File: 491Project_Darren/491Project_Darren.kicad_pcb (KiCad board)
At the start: 4 copper layers, 77 x 77 mm, 51 parts, among them J1 RJ45, J2 RJ45

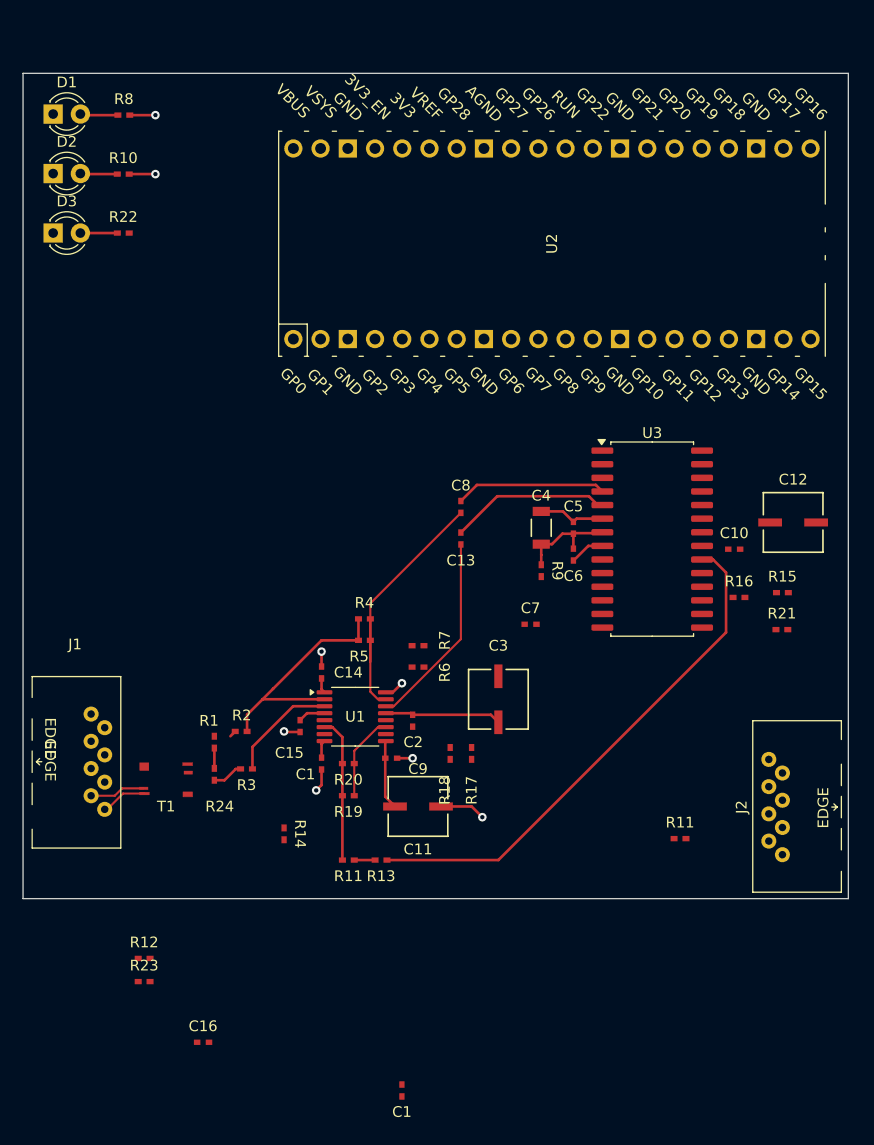
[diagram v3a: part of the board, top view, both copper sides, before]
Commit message: Added Power planes, Removed dead copper?
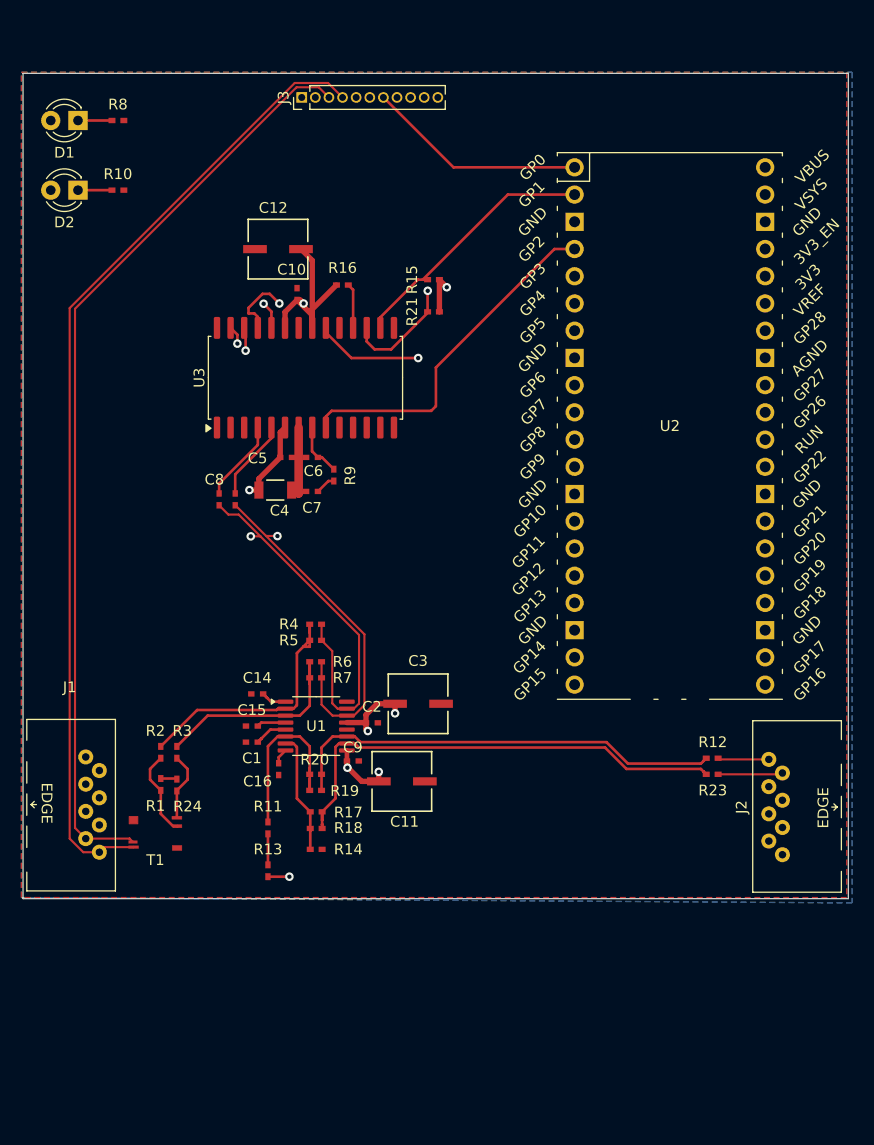
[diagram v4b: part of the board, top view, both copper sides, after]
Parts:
- removed the C1 at (142.5, 158.0)
- removed the C1 at (135.0, 127.5)
- removed D3: RED, LED_THT:LED_D3.0mm
- removed the R11 at (137.5, 136.5)
- removed R22: 1k, 491_Footprints:R_805
- added C1: 100nF, 491_Footprints:CAP_805_CER, F.Cu at (128.5, 125.5)
- added J3: Conn_01x10_MountingPin, Connector_PinHeader_1.27mm:PinHeader_1x11_P1.27mm_Vertical, F.Cu at (133.2, 65.3)
- R11: value 1k -> 100
- moved R23 56.4 mm to (171.4, 128.5)
- moved R12 56.2 mm to (171.4, 127.0)
- moved C12 54.4 mm to (130.9, 79.5), turned to 180 degrees
- moved C10 47.2 mm to (132.7, 83.7), turned to 90 degrees
- moved R16 47.1 mm to (136.9, 82.8), turned to 180 degrees
- moved R21 44.0 mm to (145.4, 85.3)
- moved R15 43.7 mm to (145.4, 82.3)
- moved R11 38.5 mm to (130.0, 133.5), turned to 90 degrees
- moved U3 35.7 mm to (133.5, 91.5), turned to 90 degrees
- moved C5 27.6 mm to (131.7, 98.9), turned to 0 degrees
- moved C16 26.4 mm to (131.0, 128.0), turned to -90 degrees
- moved C6 26.0 mm to (134.1, 98.9), turned to 180 degrees
- moved C4 25.1 mm to (130.7, 102.0), turned to 0 degrees
- moved C7 23.9 mm to (134.1, 102.1), turned to 180 degrees
- moved C8 22.6 mm to (125.4, 102.8)
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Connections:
- C7 pad 1: FILT -> Net-(C7-Pad1)
- C7 pad 2: Net-(C7-Pad2) -> GNDA
- D1 pad 1: GND -> Net-(D1-K)
- D1 pad 2: Net-(D1-A) -> +5V
- D2 pad 1: GND -> Net-(D2-K)
- D2 pad 2: Net-(D2-A) -> LED
- R10 pad 1: +5V -> Net-(D2-K)
- R10 pad 2: Net-(D2-A) -> GND
- R11 pad 1: +3V3 -> Net-(R11-Pad1)
- R11 pad 2: VCOM -> Net-(U1B-IN+)
- R8 pad 1: +5V -> Net-(D1-K)
- R8 pad 2: Net-(D1-A) -> GND
- R9 pad 1: GNDA -> Net-(C7-Pad1)
- R9 pad 2: Net-(C7-Pad2) -> FILT
- U1 pad 5: unconnected-(U1B-~{PD}-Pad5) -> Net-(U1B-~{PD})
- U2 pad 21: OLRCLK -> OSCLK
- U2 pad 22: OSCLK -> OLRCLK
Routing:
- net SIG_OUT+: track 0.00 -> 145.9 mm
- net SIG_OUT-: track 0.00 -> 142.2 mm
- net VA: track 6.26 -> 101.3 mm, vias 0 -> 1
- net SIG_IN-: track 4.31 -> 90.9 mm
- net SIG_IN+: track 5.19 -> 87.3 mm
- net LED: track 0.00 -> 77.3 mm
- net OSCLK: track 0.00 -> 76.5 mm, vias 0 -> 1
- net SDOUT: track 0.00 -> 72.7 mm, vias 0 -> 1
- net SDA: track 0.00 -> 51.1 mm, vias 0 -> 1
- net AES3-: track 18.4 -> 66.0 mm, vias 0 -> 1
- net AES3+: track 25.9 -> 72.6 mm, vias 0 -> 1
- net Net-(U1B-OUT+): track 0.00 -> 45.6 mm
- net PASS+: track 48.8 -> 93.5 mm, vias 0 -> 2
- net SCL: track 0.00 -> 44.6 mm
- net OMCLK: track 0.00 -> 34.9 mm, vias 0 -> 1
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- added copper zone on B.Cu, net +5V
- added copper zone on F.Cu, net GND
- removed copper zone on In2.Cu, net +5V
- removed copper zone on In1.Cu, net GND
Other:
- board text removed: "EDGE"

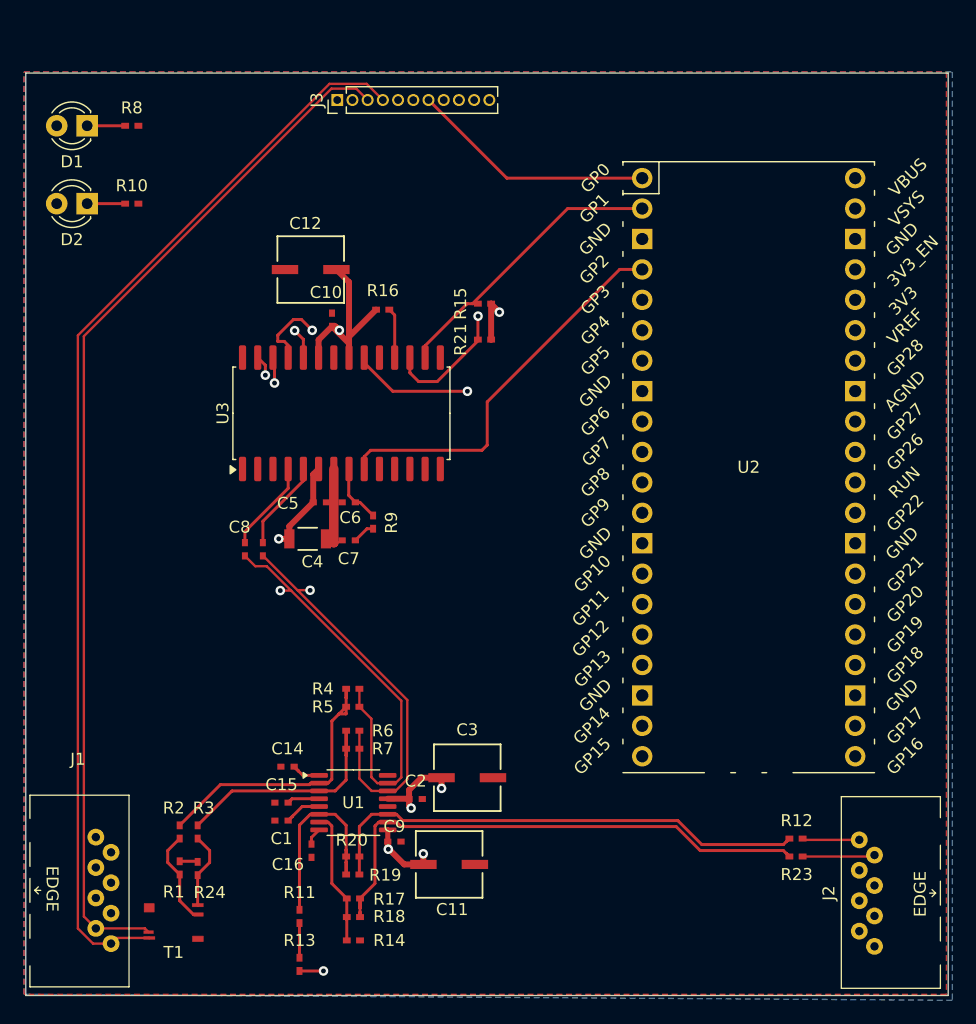
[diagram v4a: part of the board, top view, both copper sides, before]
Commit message: fix cutouts
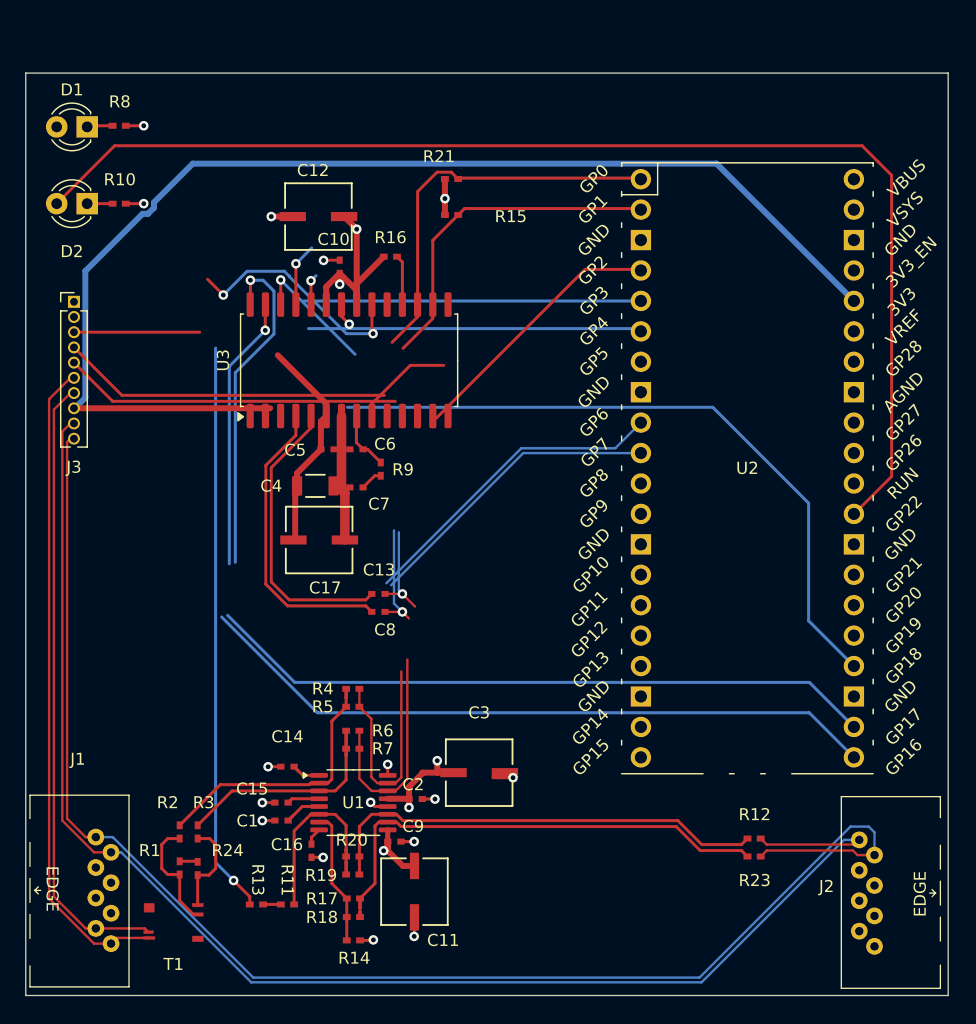
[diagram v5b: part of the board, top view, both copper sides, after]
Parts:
- added C17: 10uF, 491_Footprints:CAP_ALUM, F.Cu at (131.6, 102.1)
- J3: footprint Connector_PinHeader_1.27mm:PinHeader_1x11_P1.27mm_Vertical -> Connector_PinHeader_1.27mm:PinHeader_1x10_P1.27mm_Vertical
- moved J3 27.7 mm to (111.2, 82.2), turned to 0 degrees
- moved R21 13.7 mm to (142.7, 71.9), turned to 180 degrees
- moved C8 12.3 mm to (136.6, 108.1), turned to 180 degrees
- moved C13 10.3 mm to (136.6, 106.6), turned to 180 degrees
- moved R15 7.90 mm to (142.7, 74.9), turned to 180 degrees
- moved R13 6.16 mm to (126.4, 132.5), turned to 0 degrees
- moved C6 4.47 mm to (134.8, 94.5)
- moved C7 4.47 mm to (134.8, 97.7)
- moved C10 4.47 mm to (133.4, 79.3)
- moved C5 4.47 mm to (132.3, 94.5)
- moved R9 4.47 mm to (136.8, 96.2)
- moved U3 4.47 mm to (134.1, 87.1)
- moved C4 4.47 mm to (131.3, 97.6)
- moved R16 4.47 mm to (137.6, 78.4)
- moved C12 4.47 mm to (131.6, 75.1)
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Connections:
- J3 pad 1: VA -> unconnected-(J3-Pin_1-Pad1)
- J3 pad 10: unconnected-(J3-Pin_10-Pad10) -> SIG_OUT+
- J3 pad 3: SIG_IN+ -> PASS+
- J3 pad 4: SIG_IN- -> SDA
- J3 pad 5: SIG_OUT+ -> SCL
- J3 pad 6: SIG_OUT- -> SIG_IN-
- J3 pad 7: SDA -> SIG_IN+
- J3 pad 8: SCL -> VA
- J3 pad 9: PASS+ -> SIG_OUT-
- U2 pad 22: OLRCLK -> OLRCK
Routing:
- net OLRCK: track 0.00 -> 84.5 mm, vias 0 -> 1
- net SIG_IN-: track 90.9 -> 54.5 mm
- net SIG_IN+: track 87.3 -> 51.9 mm
- net LED: track 77.3 -> 102.2 mm
- net SIG_OUT+: track 145.9 -> 122.1 mm
- net SIG_OUT-: track 142.2 -> 119.4 mm
- net GND: track 0.04 -> 21.2 mm, vias 0 -> 16
- net VA: track 101.3 -> 119.4 mm, vias 1 -> 0
- net Net-(U3-RXP0): track 7.64 -> 24.9 mm
- net Net-(U3-RXN): track 7.55 -> 24.5 mm
- net AES3+: track 72.6 -> 55.7 mm
- net PASS+: track 93.5 -> 78.0 mm, vias 2 -> 3
- net AES3-: track 66.0 -> 52.5 mm
- net SCL: track 44.6 -> 56.7 mm
- net SDA: track 51.1 -> 60.7 mm, vias 1 -> 0
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- added copper zone on In2.Cu, net +5V
- added copper zone on In1.Cu, net GND
- removed copper zone on B.Cu, net +5V
- removed copper zone on F.Cu, net GND
